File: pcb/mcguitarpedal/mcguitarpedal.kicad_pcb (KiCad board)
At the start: 2 copper layers, 132.5 x 128 mm, 39 parts, among them J1 IN, J2 PREAMP_HEADERS, J3 BTN_MTX, J4 OUT, J5 EXP, J6 ILI9488 Module, J7 PWR_IN, J8 POTS, SW1 SW_BYPASS, SW2 SW_TUNER, SW3 SW_PRESET, SW4 LINE_LEVEL, U1 Teensy4.0_AudioShield_REVD, U2 Teensy4.1, U3 LM4562, U4 74LS148, U5 HEF4094B, U6 STPDWN-3P-5V, U7 STDN-3A24-ADJ

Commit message: Basic PCB routing
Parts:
- added D1: LED_BYPASS, LED_THT:LED_D5.0mm, F.Cu at (82.0, 133.1)
- added D2: LED_TUNER, LED_THT:LED_D5.0mm, F.Cu at (163.6, 86.1)
- added D2: LED_TUNER, LED_THT:LED_D5.0mm, F.Cu at (156.2, 85.8)
- added D2: LED_TUNER, LED_THT:LED_D5.0mm, F.Cu at (115.1, 133.6)
- added D2: LED_TUNER, LED_THT:LED_D5.0mm, F.Cu at (172.2, 85.8)
- added JP1: JP_SIGNAL_PREAMP, Connector_PinHeader_2.54mm:PinHeader_1x02_P2.54mm_Vertical, F.Cu at (138.7, 24.1)
- added R13: 150, Resistor_THT:R_Axial_DIN0207_L6.3mm_D2.5mm_P7.62mm_Horizontal, F.Cu at (86.6, 127.8)
- added R14: 150, Resistor_THT:R_Axial_DIN0207_L6.3mm_D2.5mm_P7.62mm_Horizontal, F.Cu at (120.1, 127.5)
- J1, J4, J5: footprint Connector_Audio:Jack_6.35mm_Neutrik_NMJ6HCD2_Horizontal -> mcguitarpedal:Jack_6.35mm_Neutrik_NMJ6HCD2_Horizontal_3D_MODEL
- J3: footprint Connector_PinSocket_2.54mm:PinSocket_2x08_P2.54mm_Vertical -> Connector_PinHeader_2.54mm:PinHeader_2x08_P2.54mm_Vertical
- J8: value POTS -> POT_HP_VOLUME_10k
- moved J3 18.2 mm to (140.5, 102.1), turned to 0 degrees
- moved C2 14.0 mm to (103.9, 48.8)
- moved R8 12.7 mm to (82.3, 60.2), turned to 180 degrees
- moved R9 11.3 mm to (74.7, 76.5), turned to 0 degrees
- moved R7 11.1 mm to (97.8, 78.5), turned to 90 degrees
- moved U4 10.3 mm to (135.0, 101.0)
- moved R10 9.78 mm to (86.0, 74.9), turned to 0 degrees
- moved R6 9.16 mm to (97.8, 68.1)
- moved C4 8.75 mm to (76.0, 72.9), turned to 0 degrees
- moved R5 8.68 mm to (86.0, 71.4)
- moved SW3 7.00 mm to (129.0, 127.6)
- moved C5 6.61 mm to (81.0, 67.1)
- moved U5 6.37 mm to (117.0, 121.0)
- moved RG1 5.97 mm to (98.3, 56.4), turned to 90 degrees
- moved R4 4.96 mm to (115.8, 50.3), turned to 0 degrees
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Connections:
- J1 pad T: /preamp/PREAMP_IN -> /SIGNAL_IN
- J2 pad 2: /preamp/PREAMP_IN -> /SIGNAL_IN
- J4 pad R: Net-(U1-LINE_OUT_GND) -> GND
- J4 pad S: Net-(U1-LINE_OUT_GND) -> GND
- J4 pad T: Net-(U1-LINE_OUT_R) -> Net-(J4-PadT)
- SW1 pad 1: unconnected-(SW1-Pad1) -> /SIGNAL_IN
- SW1 pad 2: unconnected-(SW1-Pad2) -> Net-(J4-PadT)
- SW1 pad 3: unconnected-(SW1-Pad3) -> /LINE_OUT
- SW1 pad 4: unconnected-(SW1-Pad4) -> /SIGNAL_IN
- SW1 pad 5: unconnected-(SW1-Pad5) -> /PREAMP_IN
- SW1 pad 6: unconnected-(SW1-Pad6) -> GND
- SW1 pad 7: unconnected-(SW1-Pad7) -> 3.3V
- SW1 pad 8: unconnected-(SW1-Pad8) -> /1_SW1
- SW1 pad 9: unconnected-(SW1-Pad9) -> GND
- SW2 pad 7: unconnected-(SW2-Pad7) -> 3.3V
- SW2 pad 8: unconnected-(SW2-Pad8) -> /2_SW2
- SW2 pad 9: unconnected-(SW2-Pad9) -> GND
- SW4 pad 1: /preamp/PREAMP_IN -> /PREAMP_IN
- SW4 pad 2: /preamp/PREAMP_IN -> /PREAMP_IN
- SW4 pad 6: /preamp/PREAMP_IN -> /PREAMP_IN
- U2 pad 2: Net-(U1-0_RX1_CRX2_CS1) -> /1_SW1
- U2 pad 37: unconnected-(U2-15_A1_RX3_SPDIF_IN-Pad37) -> /A1_VOLUME
- U2 pad 38: unconnected-(U2-16_A2_RX4_SCL1-Pad38) -> /A2_POT
- U2 pad 39: unconnected-(U2-17_A3_TX4_SDA1-Pad39) -> /A3_EXP
- U2 pad 4: Net-(U1-2_OUT2) -> /2_SW2
- U4 pad 1: Net-(J3-Pin_9) -> Net-(J3-Pin_7)
- U4 pad 10: Net-(J3-Pin_1) -> Net-(J3-Pin_15)
- U4 pad 11: Net-(J3-Pin_3) -> Net-(J3-Pin_13)
- U4 pad 12: Net-(J3-Pin_5) -> Net-(J3-Pin_11)
- U4 pad 13: Net-(J3-Pin_7) -> Net-(J3-Pin_9)
- U4 pad 2: Net-(J3-Pin_11) -> Net-(J3-Pin_5)
- U4 pad 3: Net-(J3-Pin_13) -> Net-(J3-Pin_3)
- U4 pad 4: Net-(J3-Pin_15) -> Net-(J3-Pin_1)
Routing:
- net 3.3V: track 0.00 -> 226.0 mm, vias 0 -> 2
- net /PREAMP_IN: track 0.00 -> 210.0 mm, vias 0 -> 4
- net /SIGNAL_IN: track 0.00 -> 197.4 mm, vias 0 -> 4
- net 5V: track 0.00 -> 156.4 mm, vias 0 -> 2
- net 9V: track 0.00 -> 129.2 mm
- net /preamp/STAGE1_OUT: track 0.00 -> 127.1 mm
- net /preamp/STAGE1_IN: track 0.00 -> 96.6 mm, vias 0 -> 1
- net /A1_VOLUME: track 0.00 -> 96.4 mm, vias 0 -> 1
- net /A2_POT: track 0.00 -> 96.3 mm, vias 0 -> 1
- net /A3_EXP: track 0.00 -> 84.7 mm, vias 0 -> 2
- net /37_TFT_T_IRQ: track 0.00 -> 75.8 mm, vias 0 -> 2
- net /39_TFT_MISO: track 0.00 -> 73.1 mm, vias 0 -> 1
- net Net-(J8A-Pin_1): track 0.00 -> 71.0 mm
- net /36_TOUCH_CS: track 0.00 -> 67.6 mm
- net /1_SW1: track 0.00 -> 58.8 mm
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- added copper zone on B.Cu, net GND
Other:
- board size 132.5 x 128 mm -> 132.3 x 128.5 mm

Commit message: Mostly routed board
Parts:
- removed the D2 at (163.6, 86.1)
- removed the D2 at (156.2, 85.8)
- removed the D2 at (172.2, 85.8)
- added D3: LED, LED_THT:LED_D3.0mm, F.Cu at (174.7, 62.2)
- added D4: LED, LED_THT:LED_D3.0mm, F.Cu at (174.7, 68.6)
- added D5: LED, LED_THT:LED_D3.0mm, F.Cu at (174.7, 74.9)
- added D6: LED, LED_THT:LED_D3.0mm, F.Cu at (174.7, 81.3)
- added D7: LED, LED_THT:LED_D3.0mm, F.Cu at (174.8, 36.8)
- added D8: LED, LED_THT:LED_D3.0mm, F.Cu at (174.8, 44.5)
- added JP2: JP_SCLK, Connector_PinHeader_2.54mm:PinHeader_1x02_P2.54mm_Vertical, F.Cu at (101.9, 113.3)
- added JP3: JP_MISO, Connector_PinHeader_2.54mm:PinHeader_1x02_P2.54mm_Vertical, F.Cu at (97.0, 87.9)
- added JP4: JP_MOSI, Connector_PinHeader_2.54mm:PinHeader_1x02_P2.54mm_Vertical, F.Cu at (94.2, 113.3)
- added R15: 50, Resistor_SMD:R_1206_3216Metric_Pad1.30x1.75mm_HandSolder, F.Cu at (96.8, 102.9)
- added R16: 50, Resistor_SMD:R_1206_3216Metric_Pad1.30x1.75mm_HandSolder, F.Cu at (100.6, 106.4)
- added R17: 50, Resistor_SMD:R_1206_3216Metric_Pad1.30x1.75mm_HandSolder, F.Cu at (95.8, 91.1)
- added R18: 150, Resistor_SMD:R_1206_3216Metric_Pad1.30x1.75mm_HandSolder, F.Cu at (170.9, 62.2)
- added R19: 150, Resistor_SMD:R_1206_3216Metric_Pad1.30x1.75mm_HandSolder, F.Cu at (170.9, 68.6)
- added R20: 150, Resistor_SMD:R_1206_3216Metric_Pad1.30x1.75mm_HandSolder, F.Cu at (170.7, 74.9)
- added R21: 150, Resistor_SMD:R_1206_3216Metric_Pad1.30x1.75mm_HandSolder, F.Cu at (170.7, 81.3)
- added R22: 150, Resistor_SMD:R_1206_3216Metric_Pad1.30x1.75mm_HandSolder, F.Cu at (170.9, 36.8)
- added R23: 150, Resistor_SMD:R_1206_3216Metric_Pad1.30x1.75mm_HandSolder, F.Cu at (170.9, 44.5)
- J7: footprint Connector_PinHeader_2.54mm:PinHeader_2x02_P2.54mm_Vertical -> Connector_BarrelJack:BarrelJack_Kycon_KLDX-0202-xC_Horizontal
- R13, R14: footprint Resistor_THT:R_Axial_DIN0207_L6.3mm_D2.5mm_P7.62mm_Horizontal -> Resistor_SMD:R_1206_3216Metric_Pad1.30x1.75mm_HandSolder
- U2: footprint Package_DIP:DIP-48_W15.24mm_Socket_LongPads -> mcguitarpedal:PinHeader_2x24_P2.54mm_W15.24_Vertical
- U4: value 74LS148 -> 74HC148
- U5: value HEF4094B -> 74HC4094
- moved U5 13.1 mm to (115.6, 108.0)
- moved U4 12.1 mm to (133.3, 113.0)
- moved U6 7.94 mm to (161.8, 37.8)
- moved J7 7.82 mm to (166.1, 32.3)
- moved R14 6.36 mm to (113.8, 127.8), turned to 90 degrees
- moved U7 4.32 mm to (160.5, 48.8)
- moved R13 3.04 mm to (83.6, 127.3), turned to 90 degrees
- moved D1 3.00 mm to (79.0, 133.1)
- moved D2 3.00 mm to (112.1, 133.6)
- moved SW1 3.00 mm to (59.2, 127.8)
- moved SW2 3.00 mm to (92.7, 127.6)
- moved SW3 3.00 mm to (126.0, 127.6)
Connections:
- J6 pad 10: /27_TFT_SCLK -> Net-(J6-SCK)
- J6 pad 12: /26_TFT_MOSI -> Net-(J6-SDI(MOSI))
- J6 pad 13: /39_TFT_MISO -> Net-(J6-SDO(MISO))
- J6 pad 6: /26_TFT_MOSI -> Net-(J6-SDI(MOSI))
- J6 pad 7: /27_TFT_SCLK -> Net-(J6-SCK)
- J6 pad 9: /39_TFT_MISO -> Net-(J6-SDO(MISO))
- U5 pad 13: unconnected-(U5-QP5-Pad13) -> Net-(U5-QP5)
- U5 pad 14: unconnected-(U5-QP4-Pad14) -> Net-(U5-QP4)
- U5 pad 4: unconnected-(U5-QP0-Pad4) -> Net-(U5-QP0)
- U5 pad 5: unconnected-(U5-QP1-Pad5) -> Net-(U5-QP1)
- U5 pad 6: unconnected-(U5-QP2-Pad6) -> Net-(U5-QP2)
- U5 pad 7: unconnected-(U5-QP3-Pad7) -> Net-(U5-QP3)
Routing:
- net 3.3V: track 226.0 -> 401.7 mm, vias 2 -> 5
- net Net-(J6-SDI(MOSI)): track 0.00 -> 99.4 mm, vias 0 -> 2
- net Net-(J6-SCK): track 0.00 -> 87.6 mm, vias 0 -> 2
- net /LED_STR: track 0.00 -> 77.8 mm, vias 0 -> 2
- net Net-(J6-SDO(MISO)): track 0.00 -> 72.0 mm, vias 0 -> 1
- net Net-(U5-QP0): track 0.00 -> 67.5 mm, vias 0 -> 1
- net /39_TFT_MISO: track 73.1 -> 6.50 mm, vias 1 -> 0
- net Net-(U5-QP1): track 0.00 -> 61.3 mm
- net /26_TFT_MOSI: track 68.2 -> 12.2 mm, vias 2 -> 0
- net Net-(U5-QP2): track 0.00 -> 54.5 mm
- net /27_TFT_SCLK: track 63.7 -> 9.39 mm, vias 1 -> 0
- net Net-(U2-41_A17): track 0.00 -> 51.3 mm, vias 0 -> 1
- net Net-(U5-QP3): track 0.00 -> 49.4 mm
- net Net-(U2-40_A16): track 0.00 -> 43.5 mm
- net /SCK: track 0.00 -> 42.3 mm
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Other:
- board size 132.3 x 128.5 mm -> 132 x 123 mm

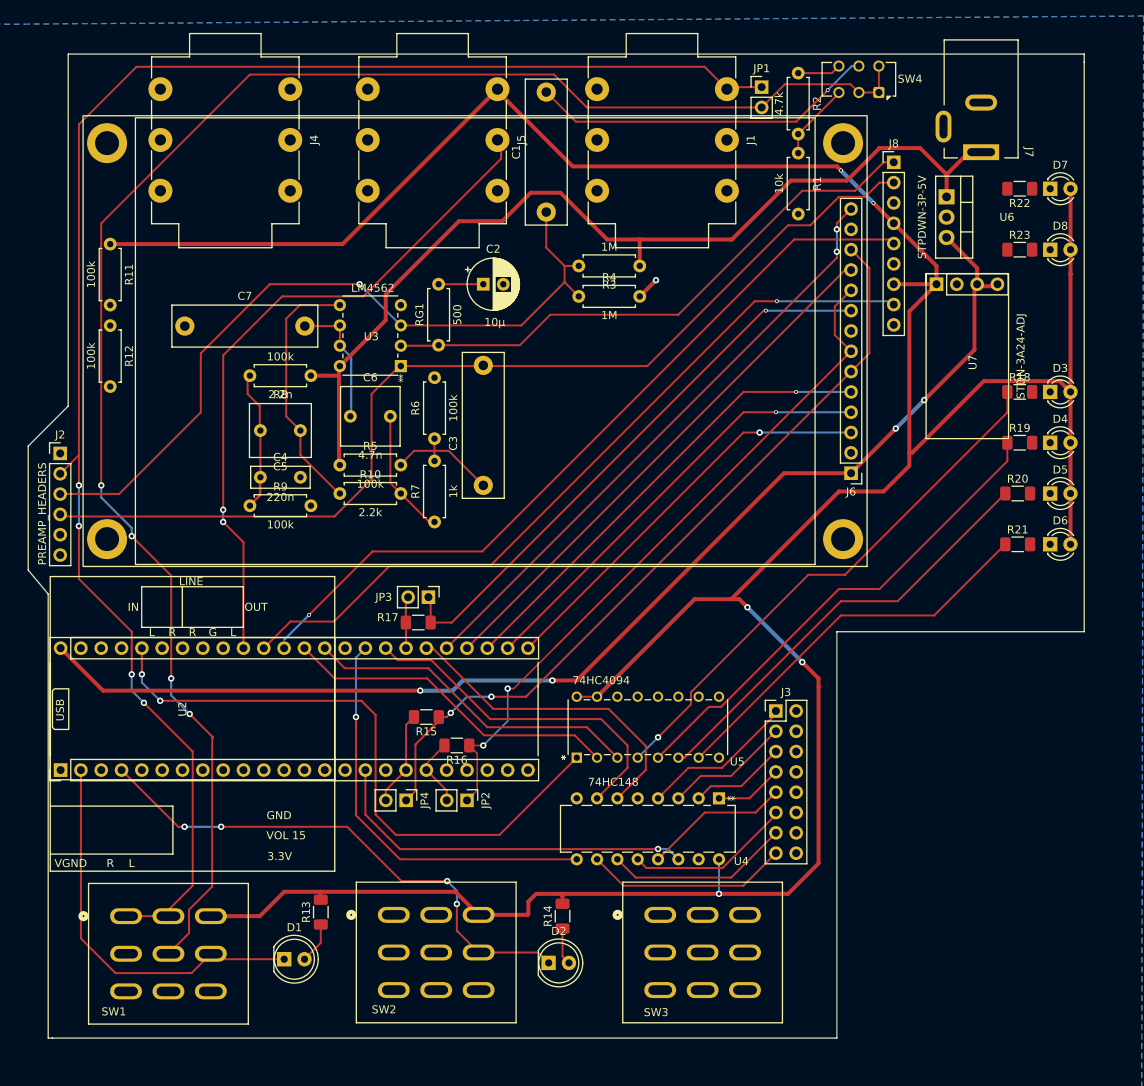
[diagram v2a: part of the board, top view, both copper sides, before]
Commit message: Reorganized power section
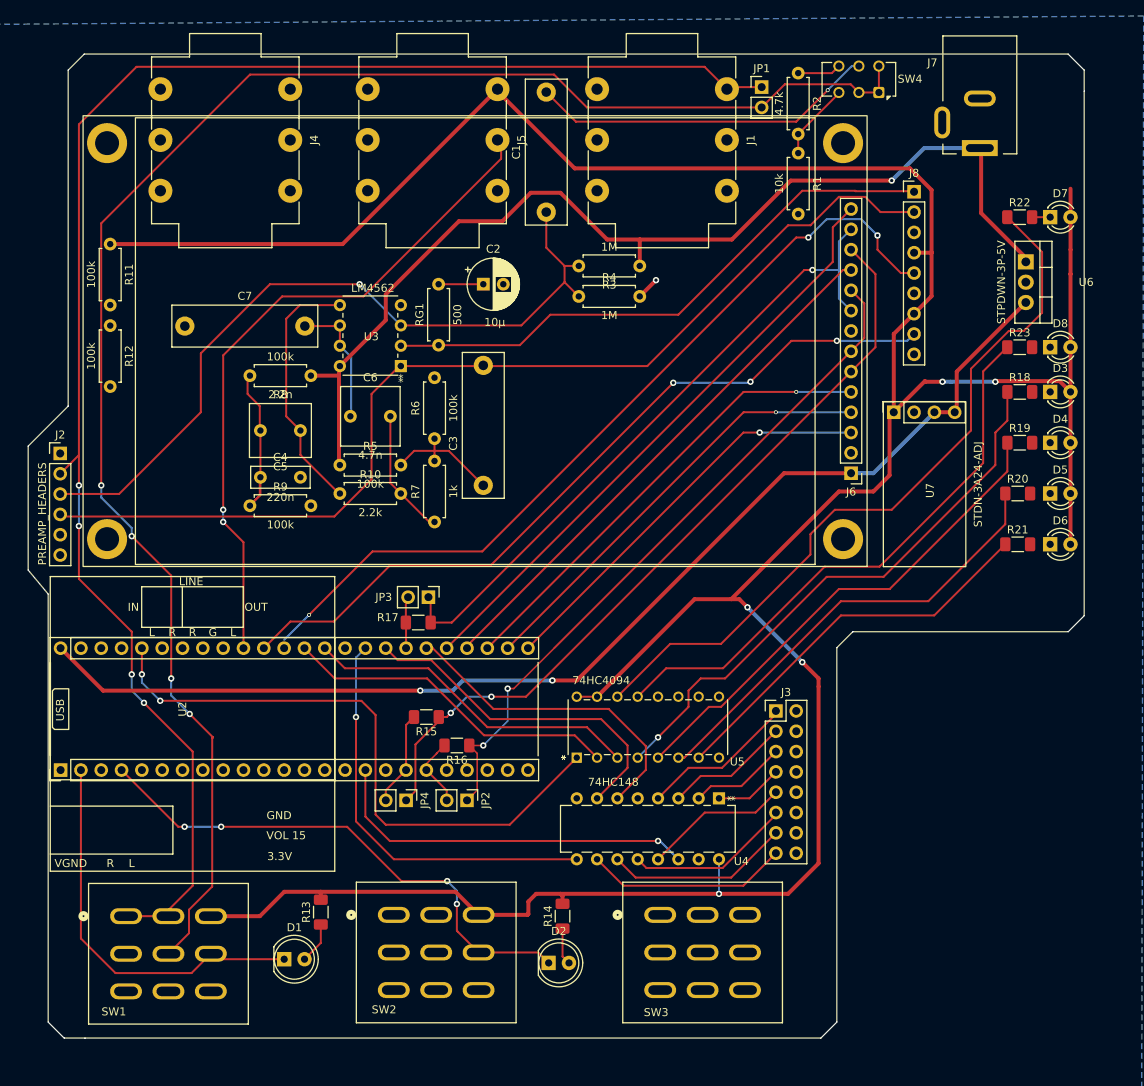
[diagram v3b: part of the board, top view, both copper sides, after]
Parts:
- moved U7 16.9 mm to (155.2, 64.8)
- moved U6 12.8 mm to (171.7, 46.0)
- moved D8 12.2 mm to (174.7, 56.6)
- moved R23 12.2 mm to (170.9, 56.6)
- moved J8 4.47 mm to (157.7, 37.2)
- moved D7 3.56 mm to (174.7, 40.4)
- moved R22 3.56 mm to (170.9, 40.4), turned to 0 degrees
- moved J7 0.53 mm to (166.0, 31.8)
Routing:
- net Net-(U5-QP4): track 0.00 -> 93.0 mm
- net Net-(U5-QP5): track 0.00 -> 71.0 mm
- net Net-(J6-SDO(MISO)): track 72.0 -> 84.0 mm
- net 9V: track 122.6 -> 133.2 mm, vias 0 -> 1
- net /A1_VOLUME: track 96.4 -> 104.4 mm, vias 1 -> 3
- net 5V: track 152.7 -> 145.8 mm, vias 4 -> 2
- net Net-(U5-QP0): track 67.5 -> 70.8 mm
- net /preamp/STAGE1_OUT: track 127.1 -> 129.7 mm
- net Net-(D7-K): track 0.00 -> 2.26 mm
- net Net-(U5-QP2): track 54.5 -> 56.8 mm
- net /A2_POT: track 96.3 -> 97.5 mm, vias 1 -> 3
- net Net-(J8A-Pin_1): track 71.0 -> 72.1 mm
- net /LED_STR: track 77.8 -> 76.8 mm
- net /36_TOUCH_CS: track 67.6 -> 68.5 mm
- net Net-(U5-QP1): track 61.3 -> 62.1 mm
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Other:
- outline, holes or cut-outs redrawn
- board text added: "TODO: Audio board 3V3 PWR LEDs Testpoints Encoders Evenly distribute jacks Mounting holes Footswitch pushbutton Switch 470n to smaller footprint"

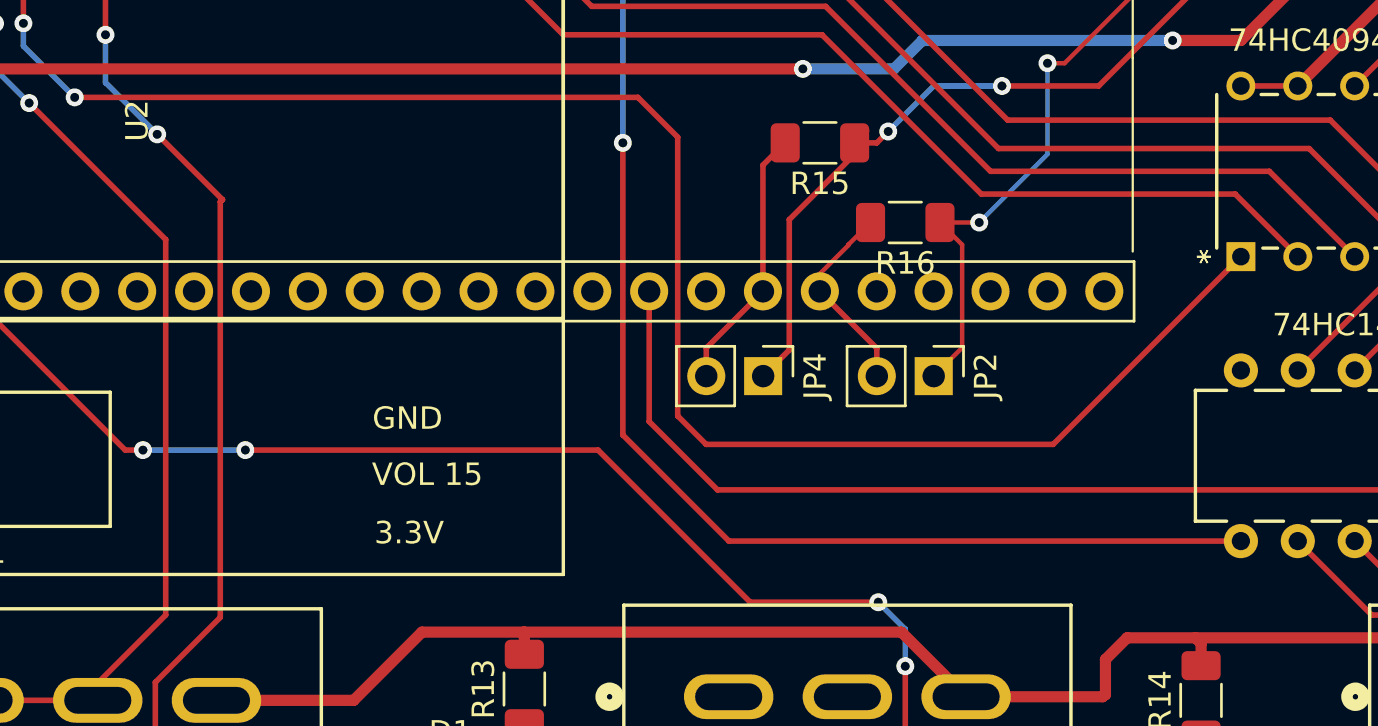
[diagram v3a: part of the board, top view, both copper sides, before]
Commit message: Encoder headers
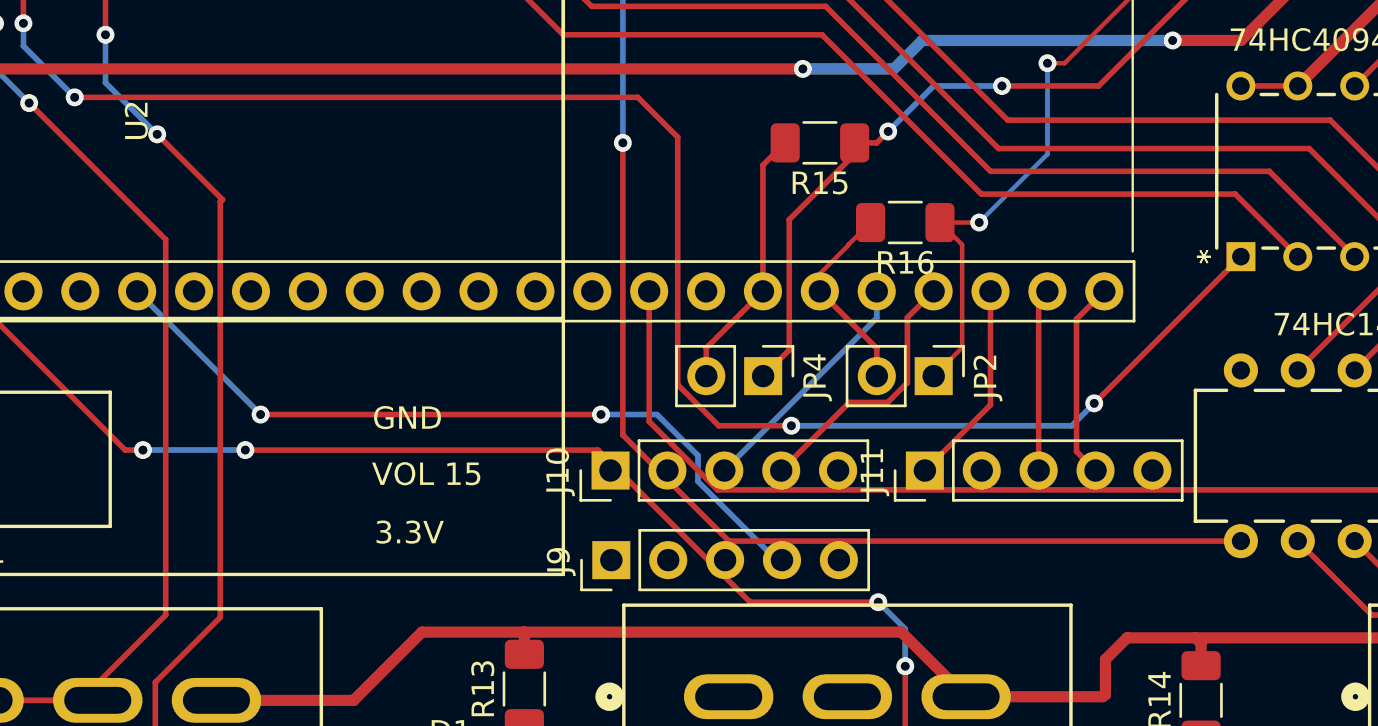
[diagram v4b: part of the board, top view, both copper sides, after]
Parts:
- added J10: ENCODER2, Connector_PinHeader_2.54mm:PinHeader_1x05_P2.54mm_Vertical, F.Cu at (87.4, 117.5)
- added J11: ENCODER3, Connector_PinHeader_2.54mm:PinHeader_1x05_P2.54mm_Vertical, F.Cu at (101.5, 117.5)
- added J9: ENCODER1, Connector_PinHeader_2.54mm:PinHeader_1x05_P2.54mm_Vertical, F.Cu at (87.5, 121.5)
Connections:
- U2 pad 17: unconnected-(U2-25_A11_RX6_SDA2-Pad17) -> /25_ENC_2_BTN
- U2 pad 20: unconnected-(U2-28_RX7-Pad20) -> /28_ENC_2_L
- U2 pad 21: unconnected-(U2-29_TX7-Pad21) -> /29_ENC_2_R
- U2 pad 22: unconnected-(U2-30_CRX3-Pad22) -> /30_ENC_3_BTN
- U2 pad 23: unconnected-(U2-31_CTX3-Pad23) -> /31_ENC_3_L
- U2 pad 24: unconnected-(U2-32_OUT1B-Pad24) -> /32_ENC_3_R
- U2 pad 5: Net-(U1-3_LRCLK2) -> /3_ENC_1_BTN
- U2 pad 6: Net-(U1-4_BCLK2) -> /4_ENC_1_L
- U2 pad 7: Net-(U1-5_IN2) -> /5_ENC_1_R
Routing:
- net /5_ENC_1_R: track 0.00 -> 34.4 mm, vias 0 -> 2
- net /29_ENC_2_R: track 0.00 -> 11.8 mm
- net /28_ENC_2_L: track 0.00 -> 10.8 mm
- net /30_ENC_3_BTN: track 0.00 -> 9.21 mm
- net /32_ENC_3_R: track 0.00 -> 8.87 mm
- net /31_ENC_3_L: track 0.00 -> 8.16 mm
- net /LED_STR: track 76.8 -> 75.3 mm, vias 2 -> 4
